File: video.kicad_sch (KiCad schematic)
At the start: 65 parts, among them IC1 MC3346, IC2 MC3346, IC3 MC3346, T1 Q_NPN_CBE, T2 Q_NPN_CBE, T3 Q_NPN_CBE, T4 Q_NPN_CBE

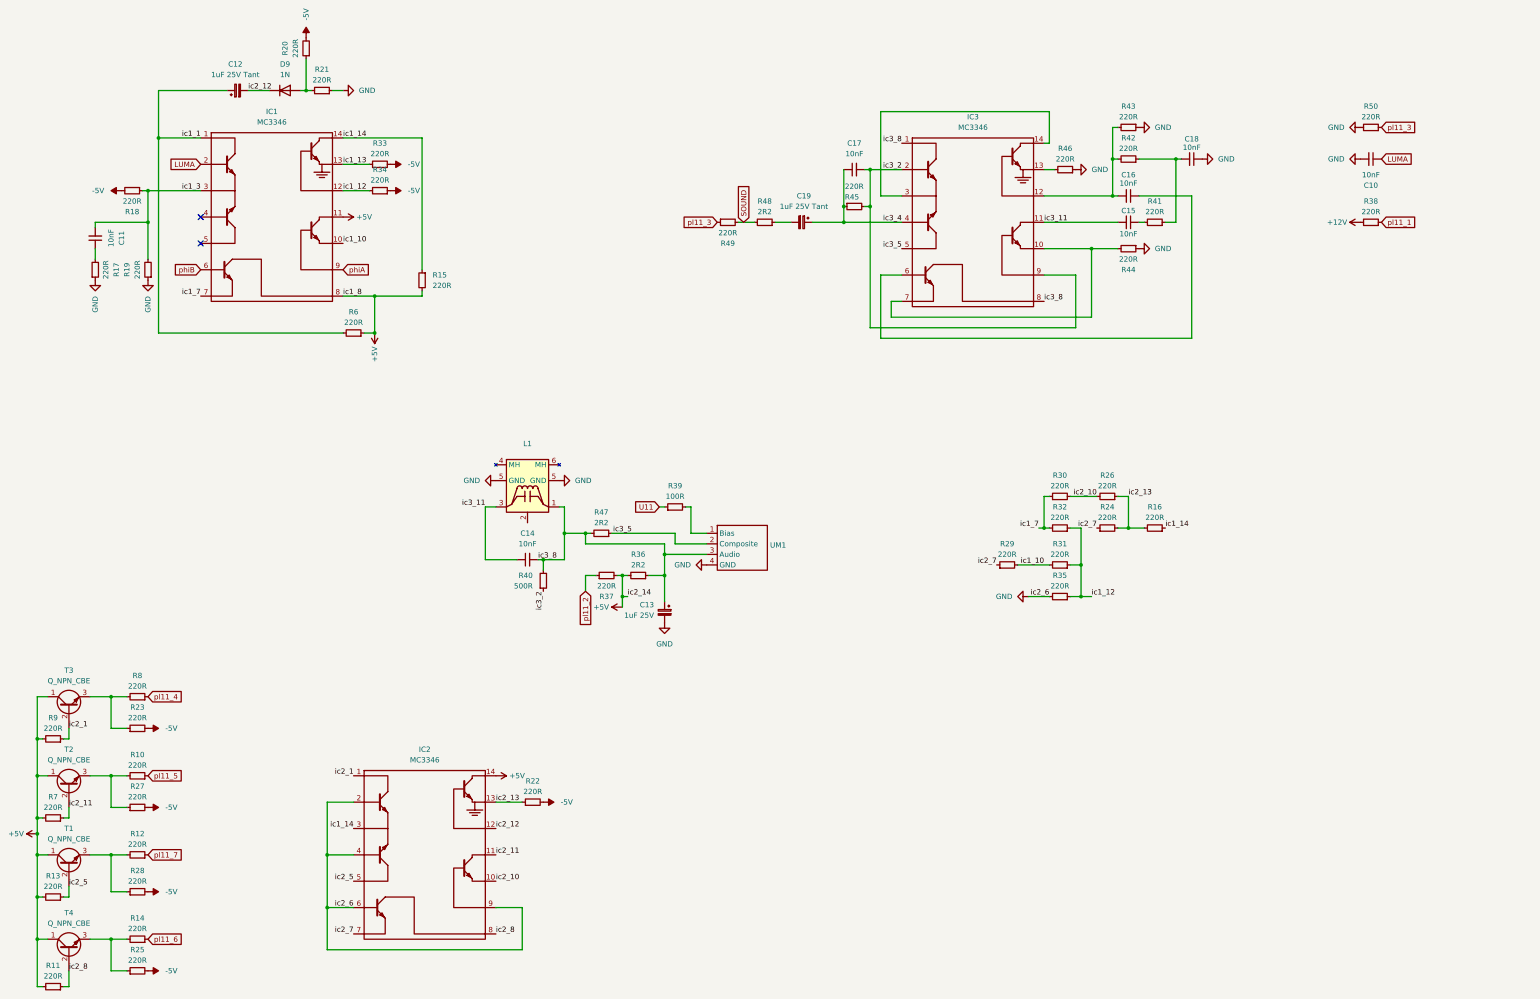
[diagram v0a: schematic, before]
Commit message: rationalise rgb circuit
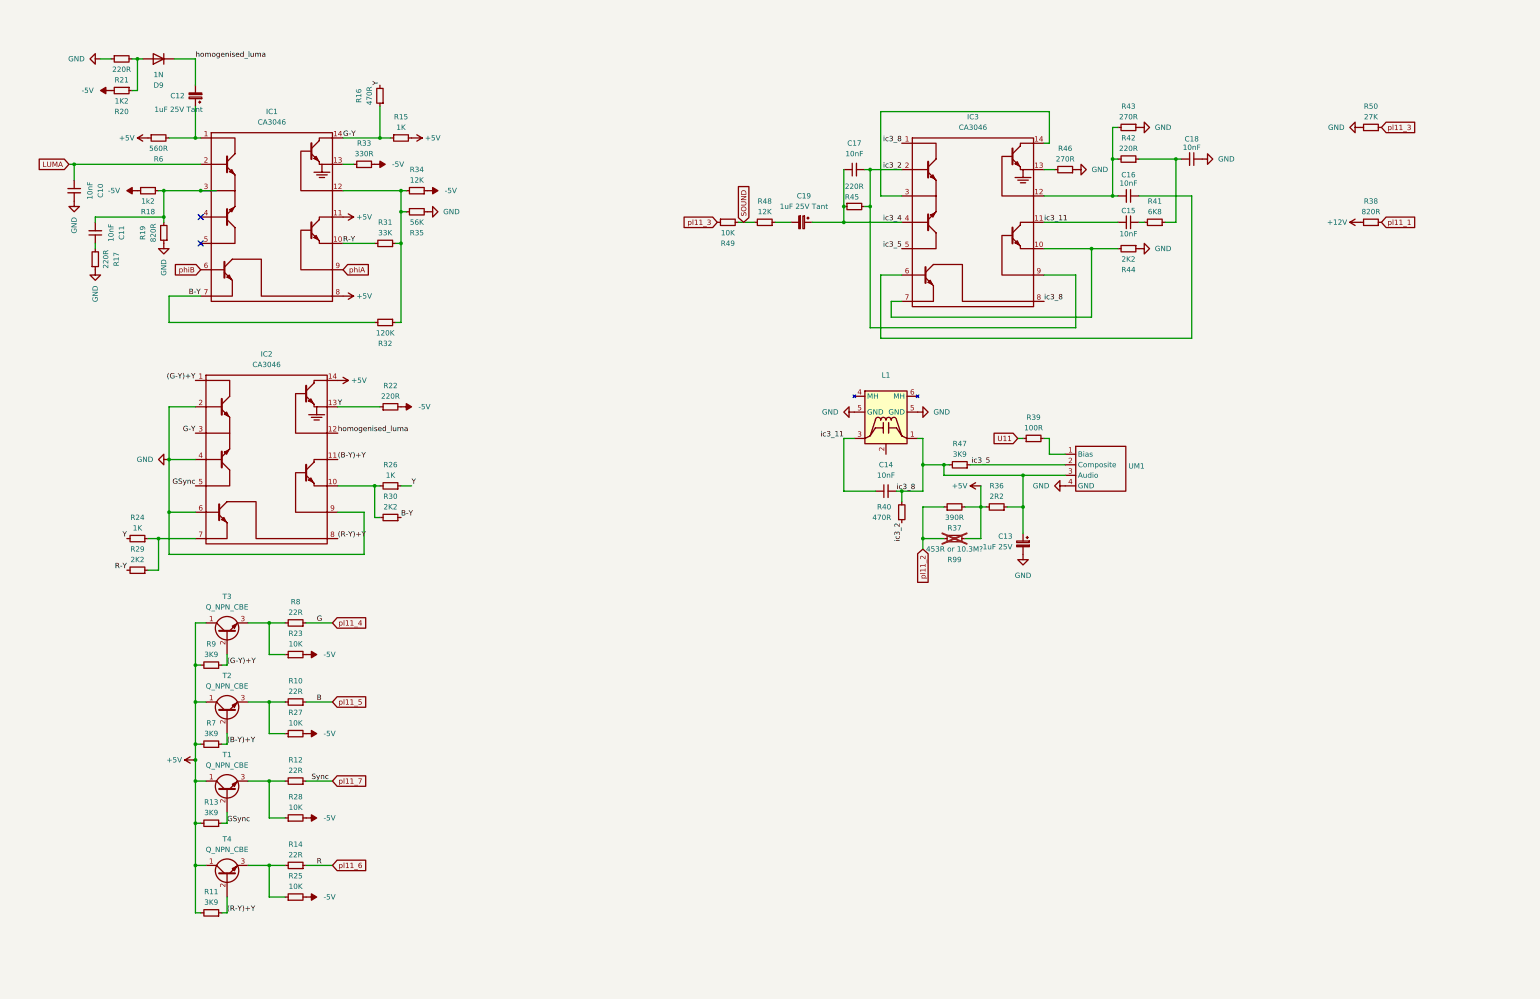
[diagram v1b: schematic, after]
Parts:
- added R99: 453R or 10.3M?, Dragon:R_Axial_DIN0309_L9.0mm_D2.5mm_P12.70mm_Horizontal, symbol Device:R_Small
- IC1, IC2, IC3: value MC3346 -> CA3046
- R10, R12, R14, R8: value 220R -> 22R
- R11, R13, R7, R9: value 220R -> 3K9
- R15, R24, R26: value 220R -> 1K
- R16: value 220R -> 470R
- R18: value 220R -> 1k2; footprint Resistor_THT:R_Axial_DIN0207_L6.3mm_D2.5mm_P10.16mm_Horizontal -> Dragon:R_Axial_DIN0207_L6.3mm_D2.5mm_P10.16mm_Horizontal
- R19, R38: value 220R -> 820R
- R20: value 220R -> 1K2; footprint Resistor_THT:R_Axial_DIN0207_L6.3mm_D2.5mm_P10.16mm_Horizontal -> Dragon:R_Axial_DIN0207_L6.3mm_D2.5mm_P10.16mm_Horizontal
- R23, R25, R27, R28, R49: value 220R -> 10K
- R29, R30, R44: value 220R -> 2K2
- R31: value 220R -> 33K
- R32: value 220R -> 120K
- R33: value 220R -> 330R
- R34: value 220R -> 12K
- R35: value 220R -> 56K
- R37: value 220R -> 390R
- R40: value 500R -> 470R
- R41: value 220R -> 6K8
- R43, R46: value 220R -> 270R
- R47: value 2R2 -> 3K9
- R48: value 2R2 -> 12K
- R50: value 220R -> 27K
- R6: value 220R -> 560R
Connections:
- net +5V: now also R99.2
- net pl11_2: now also R99.1
- net ic1_1: no longer names the net of C12.1, IC1.1, R6.2
- net ic1_10 renamed R-Y
- net ic1_12: no longer names the net of IC1.12, R31.1, R32.1, R34.2, R35.1
- net ic1_13: no longer names the net of IC1.13, R33.1
- net ic1_14 renamed G-Y
- net ic1_3: no longer names the net of C11.2, IC1.3, R18.1, R19.2
- net ic1_7 renamed B-Y
- net ic2_1 renamed (G-Y)+Y
- net ic2_10: no longer names the net of IC2.10, R26.2, R30.2
- net ic2_11 renamed (B-Y)+Y
- net ic2_12 renamed homogenised_luma
- net ic2_13 renamed Y
- net ic2_5 renamed GSync
- net ic2_7: no longer names the net of IC2.7, R24.1, R29.1
- net ic2_8 renamed (R-Y)+Y
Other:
- moved on the sheet: C10, C11, C12, C13, C14, D9, IC2, L1, R10, R11, R12, R13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

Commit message: update labelling
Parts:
- added TP1: TestPoint, TestPoint:TestPoint_THTPad_D1.0mm_Drill0.5mm, symbol Connector:TestPoint
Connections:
- net ic3_11: now also TP1.1
- net U11 renamed SECAM_COMP
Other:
- moved on the sheet: C17, R37, R39, R40, R45, R99, UM1
